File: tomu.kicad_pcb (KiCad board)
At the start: 2 copper layers, 13 x 11 mm, 16 parts, among them P1 USART0, P2 DEBUG, P3 USB-PCB, U1 EFM32HG309

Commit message: Getting closer to working.
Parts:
- removed C1: 1uF, Capacitors_SMD:C_0402
- added R5: 10k, Resistors_SMD:R_0402, B.Cu at (26.1, 19.2)
- C2: value 1uF -> 2.2uF
- C3: value 47uF -> 4.7uF
- P1: footprint debug-points -> Pin_Headers:Pin_Header_Angled_1x04
- P2: footprint usb-pcb:debug-points -> Pin_Headers:Pin_Header_Angled_1x04
- R3, R4: value 15 -> 33
- U1: value EFM32HG309 -> MKL27Z256VFM4; footprint Housings_DFN_QFN:QFN-24-1EP_5x5mm_Pitch0.65mm -> Housings_DFN_QFN:QFN-32-1EP_5x5mm_Pitch0.5mm
- W1, W2: footprint usb-pcb:minimal-points -> Measurement_Points:Test_Point_2Pads
- moved P1 14.2 mm to (18.5, 13.5)
- moved C2 3.72 mm to (20.2, 27.2), turned to 0 degrees
- moved P2 3.30 mm to (18.5, 16.1)
- moved C3 3.01 mm to (19.6, 21.8), turned to 90 degrees
- moved R4 2.61 mm to (19.2, 23.6)
- moved R3 2.18 mm to (19.2, 24.5)
- moved W1 1.55 mm to (29.0, 19.5)
- moved W2 1.14 mm to (29.1, 24.8)
- moved U1 0.24 mm to (23.3, 23.5), turned to 0 degrees
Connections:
- U1 pad 1: /LED1 -> Net-(U1-Pad1)
- U1 pad 10: /LEU0_TX -> /DBG_SWCLK
- U1 pad 11: /LEU0_RX -> /LEU0_TX
- U1 pad 12: +3V3 -> /LEU0_RX
- U1 pad 13: +3V3 -> /DBG_SWDIO
- U1 pad 14: /DEC -> Net-(R5-Pad1)
- U1 pad 15: /USB_5V -> +3V3
- U1 pad 16: +3V3 -> GND
- U1 pad 17: /RUSB_D- -> Net-(U1-Pad17)
- U1 pad 18: /RUSB_D+ -> Net-(U1-Pad18)
- U1 pad 19: /DBG_SWCLK -> Net-(U1-Pad19)
- U1 pad 2: +3V3 -> GND
- U1 pad 20: /DBG_SWDIO -> /CAP0A
- U1 pad 21: GND -> /CAP1A
- U1 pad 22: +3V3 -> Net-(U1-Pad22)
- U1 pad 23: /CAP0B -> Net-(U1-Pad23)
- U1 pad 24: /CAP1B -> Net-(U1-Pad24)
- U1 pad 25: GND -> Net-(U1-Pad25)
- U1 pad 3: /CAP0A -> /RUSB_D-
- U1 pad 4: /CAP1A -> /RUSB_D+
- U1 pad 5: /LED0 -> +3V3
- U1 pad 6: Net-(U1-Pad6) -> /USB_5V
- U1 pad 7: Net-(U1-Pad7) -> +3V3
- U1 pad 8: Net-(U1-Pad8) -> GND
- U1 pad 9: +3V3 -> Net-(U1-Pad9)
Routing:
- net +3V3: track 55.2 -> 28.9 mm
- net (no net): track 0.00 -> 19.2 mm, vias 0 -> 2
- net GND: track 31.4 -> 16.9 mm, vias 2 -> 1
- net /CAP0B: track 6.25 -> 0.00 mm, vias 1 -> 0
- net /CAP1A: track 5.37 -> 0.00 mm, vias 1 -> 0
- net /USB_5V: track 10.4 -> 13.6 mm
- net /LEU0_RX: track 3.55 -> 1.00 mm
- net /DEC: track 2.37 -> 0.00 mm
- net /USB_D-: track 8.67 -> 6.45 mm
- net /CAP0A: track 4.05 -> 2.16 mm, vias 2 -> 1
- net /CAP1B: track 7.53 -> 5.95 mm
- net /LED0: track 1.45 -> 0.18 mm
- net /LED1: track 1.74 -> 0.82 mm
- net /RUSB_D+: track 2.03 -> 1.39 mm
- net /DBG_SWDIO: track 2.07 -> 2.69 mm

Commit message: Working on the debug header.
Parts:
- removed P2: DEBUG, Pin_Headers:Pin_Header_Angled_1x04
- P1: value USART0 -> Pin_Header_Straight_2x05_Pitch1.27mm; footprint Pin_Headers:Pin_Header_Angled_1x04 -> debug-points-127mm; moved to F.Cu
- moved P1 5.97 mm to (18.4, 19.4), turned to 90 degrees
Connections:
- P1 pad 1: GND -> (no net)
- P1 pad 2: /LEU0_RX -> (no net)
- P1 pad 3: /LEU0_TX -> (no net)
- P1 pad 4: +3V3 -> (no net)
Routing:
- net Net-(U1-Pad19): track 0.00 -> 3.24 mm
- net /DBG_SWDIO: track 2.69 -> 0.00 mm
- net (no net): track 19.2 -> 17.1 mm
- net /LEU0_TX: track 1.60 -> 0.00 mm
- net /LEU0_RX: track 1.00 -> 0.00 mm
- net GND: track 16.9 -> 17.8 mm
- net +3V3: track 28.9 -> 29.7 mm

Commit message: More work...
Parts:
- removed REF**: Measurement_Point_Round-TH_Small, Measurement_Points:Measurement_Point_Round-TH_Small
- P1: value Pin_Header_Straight_2x05_Pitch1.27mm -> DEBUG; footprint debug-points-127mm -> usb-pcb:debug-points-127mm; moved to B.Cu
- moved R5 1.98 mm to (24.3, 20.1), turned to 0 degrees
- moved P1 0.54 mm to (18.8, 19.1), turned to 270 degrees
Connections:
- P1 pad 1: (no net) -> /DBG_SWCLK
- P1 pad 2: (no net) -> /LEU0_RX
- P1 pad 3: (no net) -> /LEU0_TX
- P1 pad 4: (no net) -> /DBG_SWDIO
- P1 pad 5: (no net) -> +3V3
- P1 pad 6: (no net) -> GND
- P1 pad 7: (no net) -> /RESET
- U1 pad 11: /LEU0_TX -> /LEU0_RX
- U1 pad 12: /LEU0_RX -> /LEU0_TX
- U1 pad 19: Net-(U1-Pad19) -> /RESET
- U1 pad 33: (no net) -> GND
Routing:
- net GND: track 17.8 -> 35.5 mm
- net (no net): track 17.1 -> 2.37 mm
- net /CAP1B: track 5.95 -> 0.28 mm
- net /RESET: track 0.00 -> 4.72 mm
- net Net-(U1-Pad19): track 3.24 -> 0.00 mm
- net Net-(D1-Pad1): track 0.79 -> 0.00 mm
- net +3V3: track 29.7 -> 29.6 mm, vias 3 -> 2

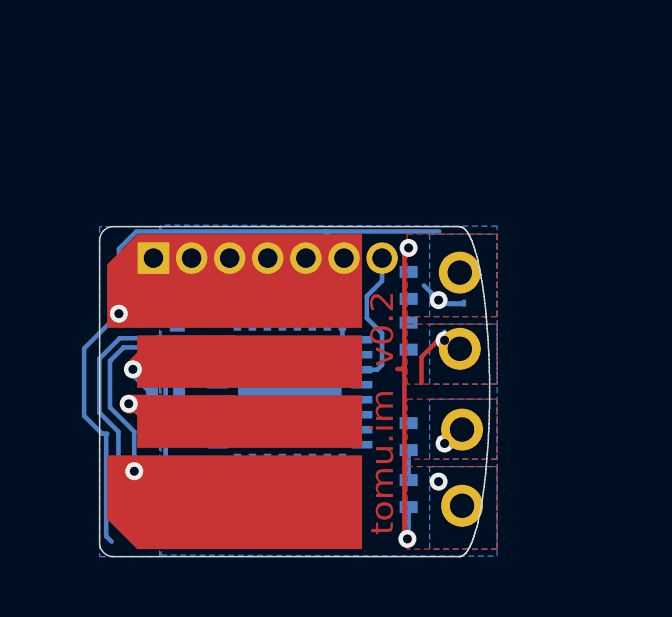
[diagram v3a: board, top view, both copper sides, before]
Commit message: Adding atecc508a part.
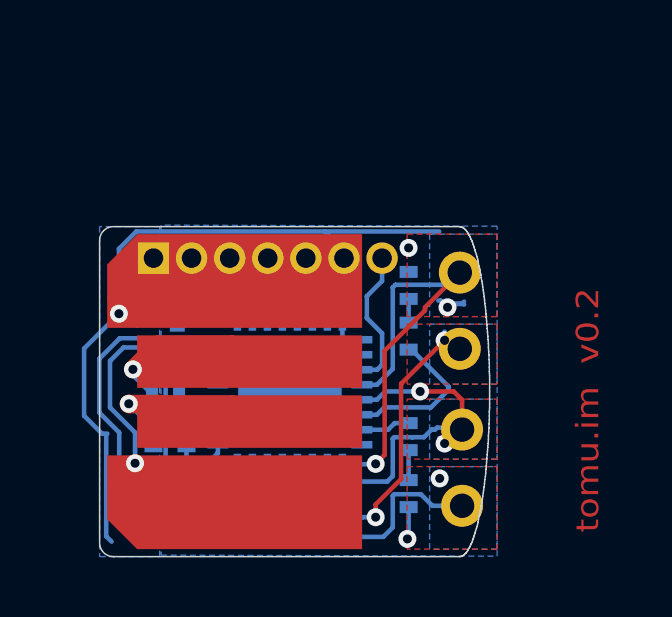
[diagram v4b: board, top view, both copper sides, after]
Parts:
- added U2: atecc508a, Housings_DFN_QFN:DFN-8-1EP_3x2mm_Pitch0.5mm, B.Cu at (20.5, 27.6)
- moved C2 2.07 mm to (19.3, 25.3)
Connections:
- U1 pad 22: Net-(U1-Pad22) -> /LED1
- U1 pad 23: Net-(U1-Pad23) -> /LED0
- U1 pad 25: Net-(U1-Pad25) -> /CAP0A
- U1 pad 26: Net-(U1-Pad26) -> /CAP1A
- U1 pad 31: Net-(U1-Pad31) -> /ASCL
- U1 pad 32: Net-(U1-Pad32) -> /ASDA
- W1 pad 1: /CAP0B -> /CAP0A
- W1 pad 2: /CAP0A -> /CAP0B
- W2 pad 1: /CAP1B -> /CAP1A
- W2 pad 2: /CAP1A -> /CAP1B
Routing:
- net /CAP0A: track 2.16 -> 15.1 mm
- net /CAP1A: track 0.00 -> 11.1 mm, vias 0 -> 1
- net +3V3: track 29.6 -> 19.1 mm, vias 2 -> 1
- net /CAP0B: track 0.00 -> 10.3 mm, vias 0 -> 2
- net /CAP1B: track 0.28 -> 8.16 mm, vias 1 -> 0
- net /LED1: track 0.00 -> 5.19 mm
- net GND: track 35.5 -> 38.7 mm
- net Net-(U2-Pad7): track 0.00 -> 2.11 mm
- net /ASDA: track 0.00 -> 1.87 mm
- net /LED0: track 0.00 -> 1.65 mm
- net Net-(U1-Pad1): track 0.00 -> 1.18 mm
- net /ASCL: track 0.00 -> 0.87 mm
- net Net-(D1-Pad1): track 0.00 -> 0.79 mm
- net (no net): track 2.37 -> 2.06 mm, vias 2 -> 4

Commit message: Temp commit before net import.
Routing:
- net (no net): track 2.06 -> 2.93 mm
- net /ASCL: track 0.87 -> 0.00 mm
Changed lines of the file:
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@@
-(kicad_pcb (version 4) (host pcbnew 4.0.4-stable)
+(kicad_pcb (version 4) (host pcbnew 4.0.4+e1-6308~48~ubuntu14.04.1-stable)
   (general
     (links 51)
-    (no_connects 24)
-    (area 16.97489 17.974999 30.025001 29.02511)
+    (no_connects 22)
+    (area 9.247287 15.822599 139.107141 45.2)
     (thickness 1.6)
     (drawings 176)
@@
   (segment (start 27.16 18.85) (end 27.3 18.71) (width 0.1524) (layer F.Cu) (net 0))
   (via (at 27.3 18.71) (size 0.6) (drill 0.3) (layers F.Cu B.Cu) (net 0))
+  (segment (start 22.606 27.051) (end 22.606 26.543) (width 0.1524) (layer B.Cu) (net 0))
+  (segment (start 22.348 27.309) (end 22.606 27.051) (width 0.1524) (layer B.Cu) (net 0))
   (segment (start 19.071 26.809) (end 19.296 26.809) (width 0.1524) (layer B.Cu) (net 1))
   (segment (start 19.296 26.809) (end 19.88819 26.21681) (width 0.1524) (layer B.Cu) (net 1))
@@
   (segment (start 23.114 27.305) (end 23.114 26.543) (width 0.1524) (layer B.Cu) (net 32))
   (segment (start 22.61 27.809) (end 23.114 27.305) (width 0.1524) (layer B.Cu) (net 32))
-  (segment (start 22.606 27.051) (end 22.606 26.543) (width 0.1524) (layer B.Cu) (net 33))
-  (segment (start 22.348 27.309) (end 22.606 27.051) (width 0.1524) (layer B.Cu) (net 33))
   (segment (start 20.9466 26.289) (end 20.193 26.289) (width 0.1524) (layer B.Cu) (net 34))
   (segment (start 21.5926 25.9204) (end 21.3152 25.9204) (width 0.1524) (layer B.Cu) (net 34))
@@
     (connect_pads (clearance 0.1524))
     (min_thickness 0.1524)
-    (fill (arc_segments 16) (thermal_gap 0.1524) (thermal_bridge_width 0.1525) (smoothing chamfer))
+    (fill yes (arc_segments 16) (thermal_gap 0.1524) (thermal_bridge_width 0.1525) (smoothing chamfer))
     (polygon
       (pts
@@
     (connect_pads yes (clearance 0))
     (min_thickness 0.254)
-    (fill (arc_segments 16) (thermal_gap 0.508) (thermal_bridge_width 0.508))
+    (fill yes (arc_segments 16) (thermal_gap 0.508) (thermal_bridge_width 0.508))
     (polygon
       (pts
@@
     (connect_pads yes (clearance 0))
     (min_thickness 0.254)
-    (fill (arc_segments 16) (thermal_gap 0.508) (thermal_bridge_width 0.508))
+    (fill yes (arc_segments 16) (thermal_gap 0.508) (thermal_bridge_width 0.508))
     (polygon
       (pts
@@
     (connect_pads yes (clearance 0))
     (min_thickness 0.254)
-    (fill (arc_segments 16) (thermal_gap 0.508) (thermal_bridge_width 0.508))
+    (fill yes (arc_segments 16) (thermal_gap 0.508) (thermal_bridge_width 0.508))
     (polygon
       (pts
@@
     (connect_pads yes (clearance 0))
     (min_thickness 0.254)
-    (fill (arc_segments 16) (thermal_gap 0.508) (thermal_bridge_width 0.508))
+    (fill yes (arc_segments 16) (thermal_gap 0.508) (thermal_bridge_width 0.508))
     (polygon
       (pts
@@
     (connect_pads yes (clearance 0))
     (min_thickness 0.254)
-    (fill (arc_segments 16) (thermal_gap 0.508) (thermal_bridge_width 0.508))
+    (fill yes (arc_segments 16) (thermal_gap 0.508) (thermal_bridge_width 0.508))
     (polygon
       (pts
@@
     (connect_pads yes (clearance 0))
     (min_thickness 0.254)
-    (fill (arc_segments 16) (thermal_gap 0.508) (thermal_bridge_width 0.508))
+    (fill yes (arc_segments 16) (thermal_gap 0.508) (thermal_bridge_width 0.508))
     (polygon
       (pts
@@
     (connect_pads yes (clearance 0))
     (min_thickness 0.254)
-    (fill (arc_segments 16) (thermal_gap 0.508) (thermal_bridge_width 0.508))
+    (fill yes (arc_segments 16) (thermal_gap 0.508) (thermal_bridge_width 0.508))
     (polygon
       (pts
@@
     (connect_pads yes (clearance 0))
     (min_thickness 0.254)
-    (fill (arc_segments 16) (thermal_gap 0.508) (thermal_bridge_width 0.508))
+    (fill yes (arc_segments 16) (thermal_gap 0.508) (thermal_bridge_width 0.508))
     (polygon
       (pts
@@
     (connect_pads (clearance 0.1524))
     (min_thickness 0.1524)
-    (fill (arc_segments 16) (thermal_gap 0.1524) (thermal_bridge_width 0.1525) (smoothing chamfer))
+    (fill yes (arc_segments 16) (thermal_gap 0.1524) (thermal_bridge_width 0.1525) (smoothing chamfer))
     (polygon
       (pts

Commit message: Another temp commit.
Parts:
- U2: value atecc508a -> ateccXXXa
- moved C2 2.36 mm to (17.8, 27.1), turned to 270 degrees
- moved R3 0.77 mm to (19.8, 25.0), turned to 90 degrees
- moved R4 0.60 mm to (19.8, 23.5), turned to 270 degrees
- moved U2 0.28 mm to (20.8, 27.6)
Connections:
- U1 pad 1: Net-(U1-Pad1) -> /ASPI_MISO
- U1 pad 29: Net-(U1-Pad29) -> /ASPI_CS
- U1 pad 30: Net-(U1-Pad30) -> /ASPI_SCK
- U1 pad 31: /ASCL -> /ASPI_MOSI
- U1 pad 32: /ASDA -> GND
- U2 pad 1: Net-(U2-Pad1) -> /ASPI_CS
- U2 pad 2: Net-(U2-Pad2) -> /ASPI_MISO
- U2 pad 5: /ASDA -> /ASPI_MOSI
- U2 pad 6: /ASCL -> /ASPI_SCK
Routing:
- net +3V3: track 19.1 -> 40.0 mm
- net GND: track 38.7 -> 45.3 mm
- net /ASPI_MISO: track 0.00 -> 5.06 mm
- net (no net): track 2.93 -> 0.03 mm, vias 4 -> 2
- net Net-(U2-Pad7): track 2.11 -> 0.00 mm
- net /ASPI_SCK: track 0.00 -> 2.07 mm
- net /ASDA: track 1.87 -> 0.00 mm
- net /USB_5V: track 13.8 -> 12.3 mm
- net /ASPI_CS: track 0.00 -> 1.51 mm
- net /USB_D+: track 5.57 -> 4.16 mm
- net Net-(U1-Pad1): track 1.18 -> 0.00 mm
- net /ASPI_MOSI: track 0.00 -> 0.83 mm

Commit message: More improvements.
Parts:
- moved C2 5.41 mm to (17.8, 21.6), turned to 90 degrees
- moved P1 0.22 mm to (18.6, 19.2)
- moved R5 0.19 mm to (24.5, 20.2)
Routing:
- net GND: track 45.3 -> 27.0 mm, vias 1 -> 2
- net +3V3: track 40.0 -> 44.3 mm
- net /LEU0_RX: track 0.00 -> 3.80 mm
- net /LEU0_TX: track 0.00 -> 3.03 mm
- net /DBG_SWDIO: track 0.00 -> 2.43 mm
- net /DBG_SWCLK: track 2.58 -> 4.84 mm
- net /LED1: track 5.19 -> 3.69 mm
- net Net-(R5-Pad1): track 0.00 -> 0.86 mm
- net /CAP1B: track 8.16 -> 7.39 mm
- net /CAP0B: track 10.6 -> 10.7 mm, vias 2 -> 1
- net (no net): track 0.03 -> 0.00 mm, vias 2 -> 1
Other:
- board text added: "+"
- board text added: "G"
- board text added: "N"

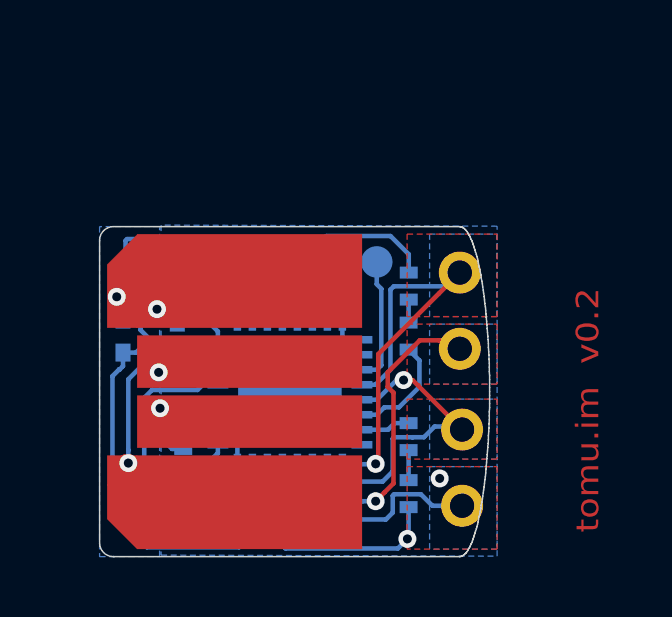
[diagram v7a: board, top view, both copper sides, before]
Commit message: Fully routed design which passes DRC.
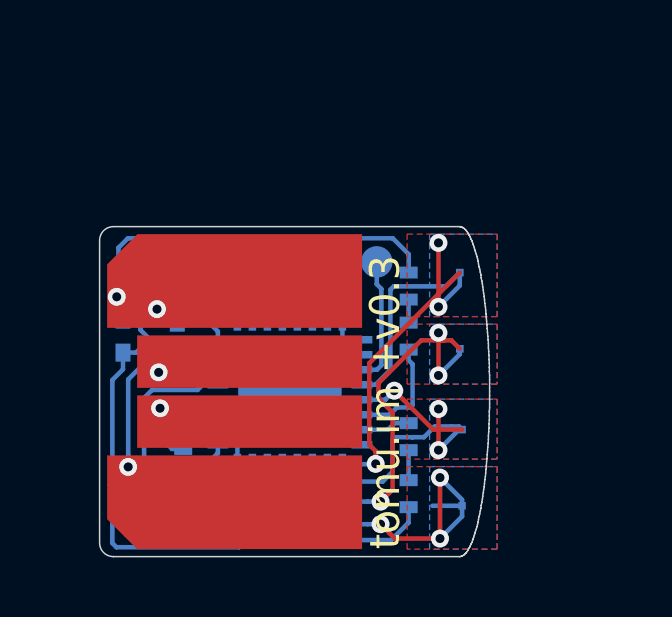
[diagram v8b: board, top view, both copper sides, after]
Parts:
- added JP1: Jumper_NO_Small, Resistors_SMD:R_0402, B.Cu at (22.0, 30.3)
- W1, W2: footprint Measurement_Points:Test_Point_2Pads -> usb-pcb:cap-points
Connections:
- U1 pad 29: /ASPI_CS -> /ASPI_CS1
- U2 pad 1: /ASPI_CS -> /ASPI_CS2
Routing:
- net /CAP1B: track 7.39 -> 11.7 mm, vias 0 -> 3
- net /CAP0A: track 15.0 -> 18.8 mm, vias 1 -> 3
- net /CAP0B: track 10.7 -> 13.6 mm, vias 1 -> 3
- net /CAP1A: track 11.2 -> 13.3 mm, vias 1 -> 3
- net /ASPI_CS1: track 0.00 -> 2.06 mm
- net /ASPI_CS: track 1.51 -> 0.00 mm
- net /ASPI_CS2: track 0.00 -> 1.29 mm
- net GND: track 27.0 -> 27.8 mm
- net +3V3: track 44.3 -> 44.6 mm, vias 1 -> 0
- net (no net): vias 1 -> 0
- removed copper zone on B.Cu, net +3V3
- removed copper zone on B.Cu, net GND
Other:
- board text added: "tomu.im +v0.3"
- board text removed: "tomu.im v0.2"
